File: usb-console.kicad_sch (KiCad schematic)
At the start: 31 parts, among them J9 USB-C_USB-310F-B-SU, U3 FT230XQ-R, U4 NTS0102DP

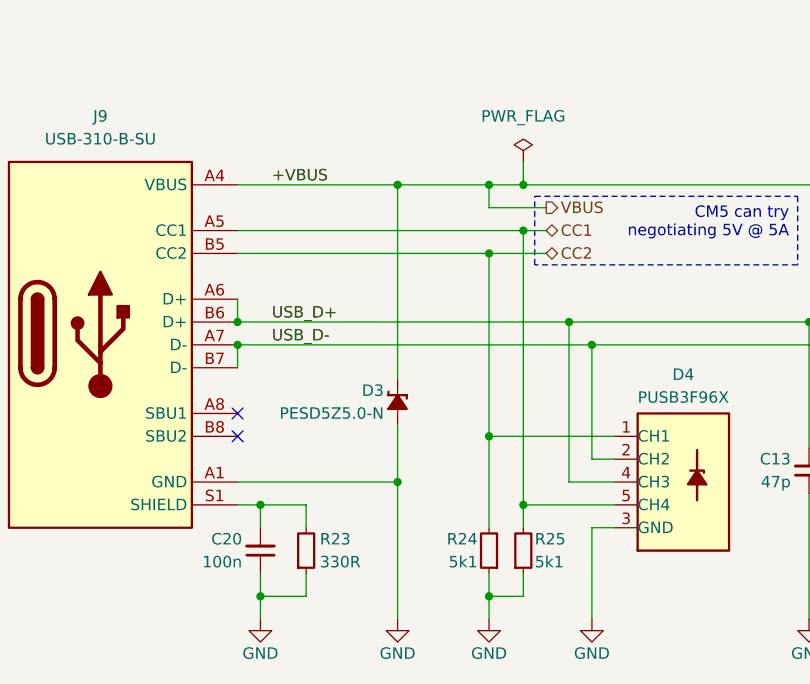
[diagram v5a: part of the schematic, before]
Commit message: [#1] WIP: Refactor schematic
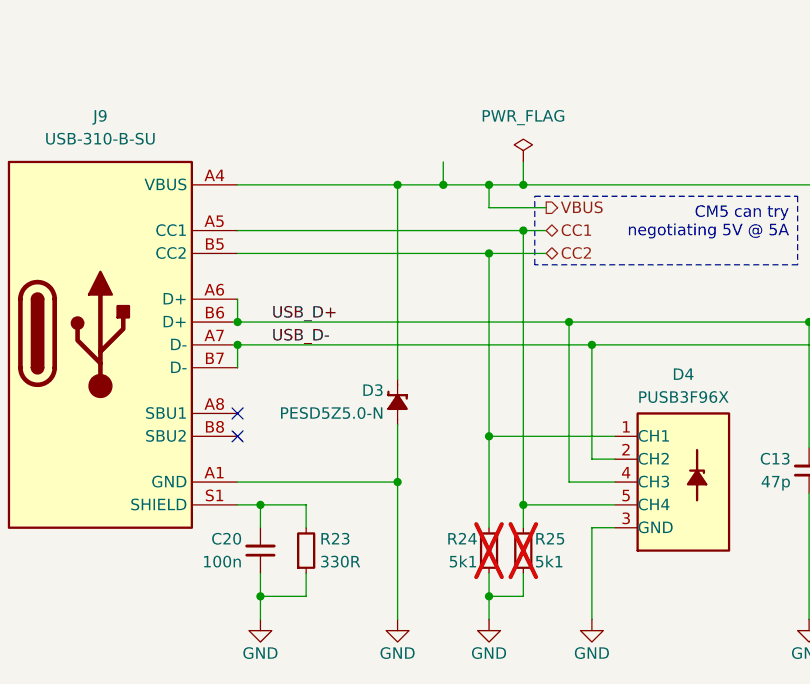
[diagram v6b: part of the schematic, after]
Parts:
- R24, R25: now not fitted
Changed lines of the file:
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@@
 	)
 	(junction
+		(at 107.95 127)
+		(diameter 0)
+		(color 0 0 0 0)
+	)
+	(junction
 		(at 148.59 142.24)
 		(diameter 0)
@@
 	(wire
 		(pts
+			(xy 107.95 124.46) (xy 107.95 127)
+		)
+		(stroke
+			(width 0)
+			(type default)
+		)
+	)
+	(wire
+		(pts
 			(xy 261.62 161.29) (xy 264.16 161.29)
 		)
@@
 	(wire
 		(pts
+			(xy 107.95 127) (xy 113.03 127)
+		)
+		(stroke
+			(width 0)
+			(type default)
+		)
+	)
+	(wire
+		(pts
 			(xy 185.42 175.26) (xy 185.42 161.29)
 		)
@@
 	(wire
 		(pts
-			(xy 102.87 127) (xy 113.03 127)
+			(xy 102.87 127) (xy 107.95 127)
 		)
 		(stroke
@@
 		)
 	)
-	(label "+VBUS"
-		(at 88.9 127 0)
-		(effects
-			(font
-				(size 1.27 1.27)
-			)
-			(justify left bottom)
-		)
-	)
 	(label "FTDI_CBUS3"
 		(at 252.73 153.67 0)
@@
 		(length 2.54)
 		(shape round)
+		(at 107.95 124.46 0)
+		(effects
+			(font
+				(size 1.27 1.27)
+			)
+			(justify left bottom)
+		)
+		(property "Netclass" "PWR"
+			(at 107.95 119.634 0)
+			(effects
+				(font
+					(size 1.27 1.27)
+				)
+			)
+		)
+		(property "Component Class" ""
+			(at -143.51 -45.72 0)
+			(effects
+				(font
+					(size 1.27 1.27)
+					(italic yes)
+				)
+			)
+		)
+	)
+	(netclass_flag ""
+		(length 2.54)
+		(shape round)
 		(at 203.2 138.43 0)
 		(effects
@@
 		(in_bom yes)
 		(on_board yes)
-		(dnp no)
+		(dnp yes)
 		(property "Reference" "R24"
 			(at 111.76 166.37 90)
@@
 		(in_bom yes)
 		(on_board yes)
-		(dnp no)
+		(dnp yes)
 		(property "Reference" "R25"
 			(at 118.11 166.37 90)

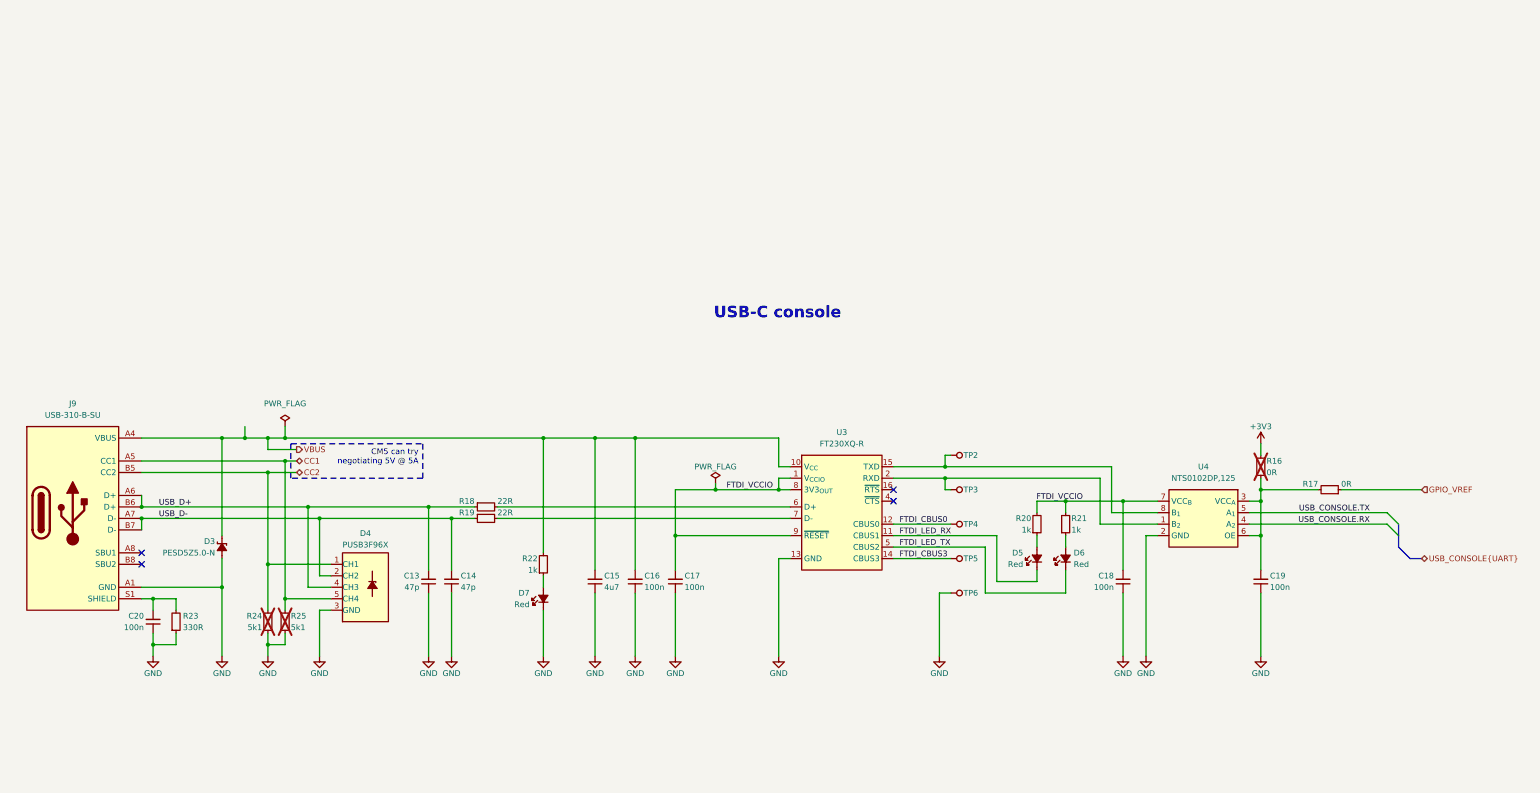
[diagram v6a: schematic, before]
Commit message: [#3] WIP: Clear ERC, re-annotate schematic
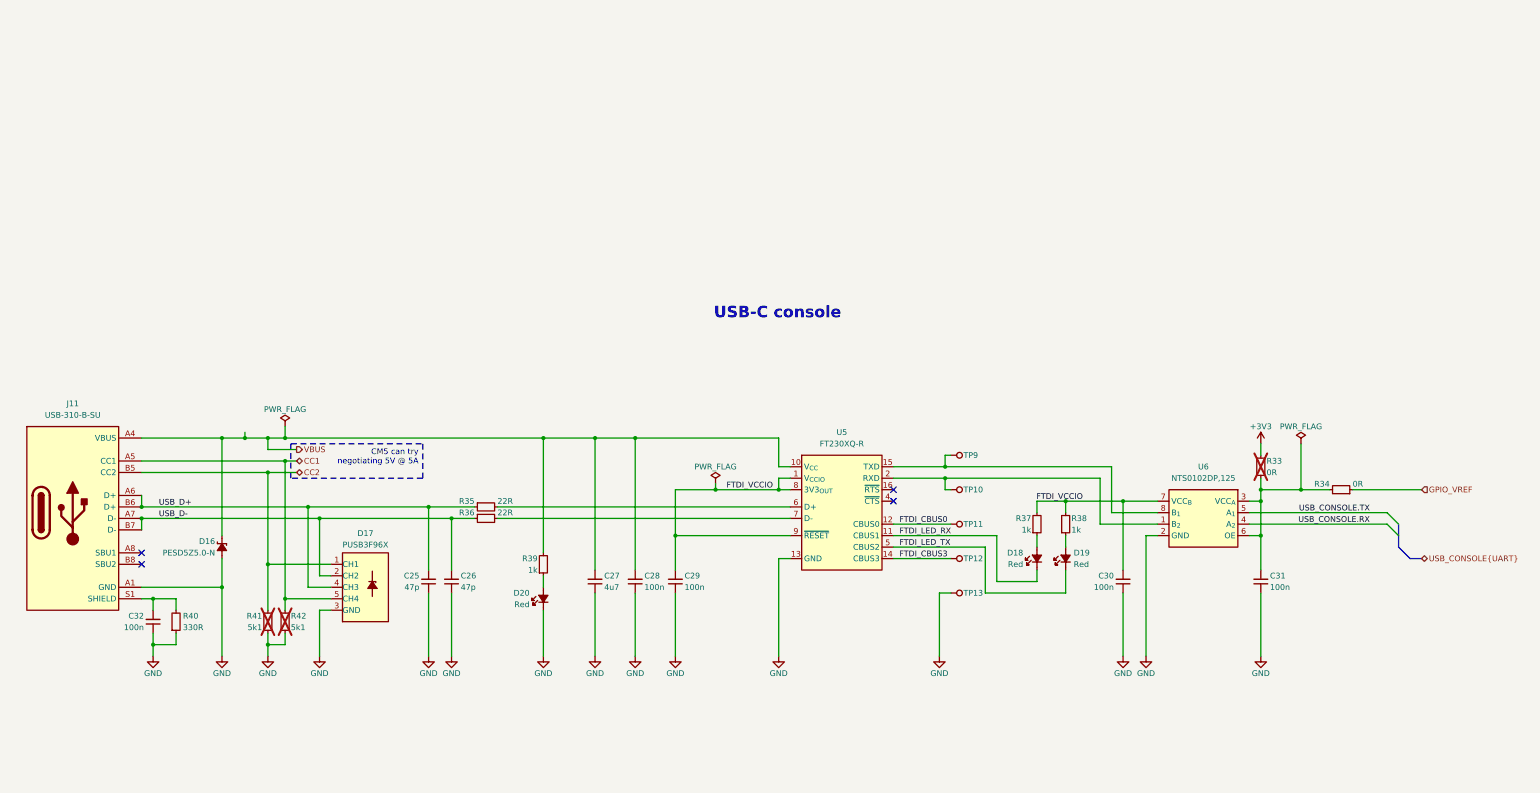
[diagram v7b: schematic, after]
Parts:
- renumbered C13 to C25, C14 to C26, C15 to C27, C16 to C28, C17 to C29, C18 to C30, C19 to C31, C20 to C32, D3 to D16, D4 to D17, D5 to D18, D6 to D19, D7 to D20, J9 to J11, R16 to R33, R17 to R34, R18 to R35, R19 to R36, R20 to R37, R21 to R38, R22 to R39, R23 to R40, R24 to R41, R25 to R42, TP3 to TP10, TP4 to TP11, TP5 to TP12, TP6 to TP13, TP2 to TP9, U3 to U5, U4 to U6
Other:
- moved on the sheet: R34

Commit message: [#3] Start USB layout
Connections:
- net D+: now reaches R35.2, U5.6 (D+)
- net D-: now reaches R36.2, U5.7 (D-)
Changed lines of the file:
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@@
+		)
+	)
+	(label "D-"
+		(at 226.06 144.78 180)
+		(effects
+			(font
+				(size 1.27 1.27)
+			)
+			(justify right bottom)
 		)
 	)
@@
 		)
 	)
+	(label "D+"
+		(at 226.06 142.24 180)
+		(effects
+			(font
+				(size 1.27 1.27)
+			)
+			(justify right bottom)
+		)
+	)
